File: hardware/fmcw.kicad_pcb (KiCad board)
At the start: 4 copper layers, 147.8 x 58.9 mm, 414 parts, among them CON1 BARREL_JACK, J1 SD_Card, J2 USB_B_Micro, J3 SMA, J4 SMA, J5 SMA, P1 CONN_02X04, P2 CONN_02X04, Q1 DNP(RE1C002UN), Q2 RE1C002UN, SW1 SW_PUSH, U1 LP5907MFX-3.3, U10 LP5907MFX-3.0, U11 LTC2292, U12 ADF4158, U13 TLV172DCK, U14 PAT1220-3dB, U15 HMC431LP4, U16 PD4859J5050S2HF, U17 PAT1220-5dB, U18 SE5004L, U19 DC4759J5020AHF, U2 LP5907MFX-1.8, U20 PAT1220-6dB, U22 TRF37A73, U23 SKY65404, U24 TRF37A73, U25 SKY65404, U26 TPS5420D, U27 TPS5420D, U28 TPS560200, U29 LP2985A-10DBVR, U3 KT2520K-T, U30 TPS7A7001DDA, U31 TPS7A91, U32 TPS7A91, U33 LP5907MFX-3.0, U34 TPS7A91, U35 5400BL15B050E, U36 5400BL15B050E, U37 5400BL15B050E, U38 ADL5802, U39 ADA4940-2, U4 NC7SVU04P5X, U5 NB3N551, U6 XC7A15T-FTG256, U7 W25Q32JV, U8 93LCxxB, U9 FT2232H, Y1 12MHz

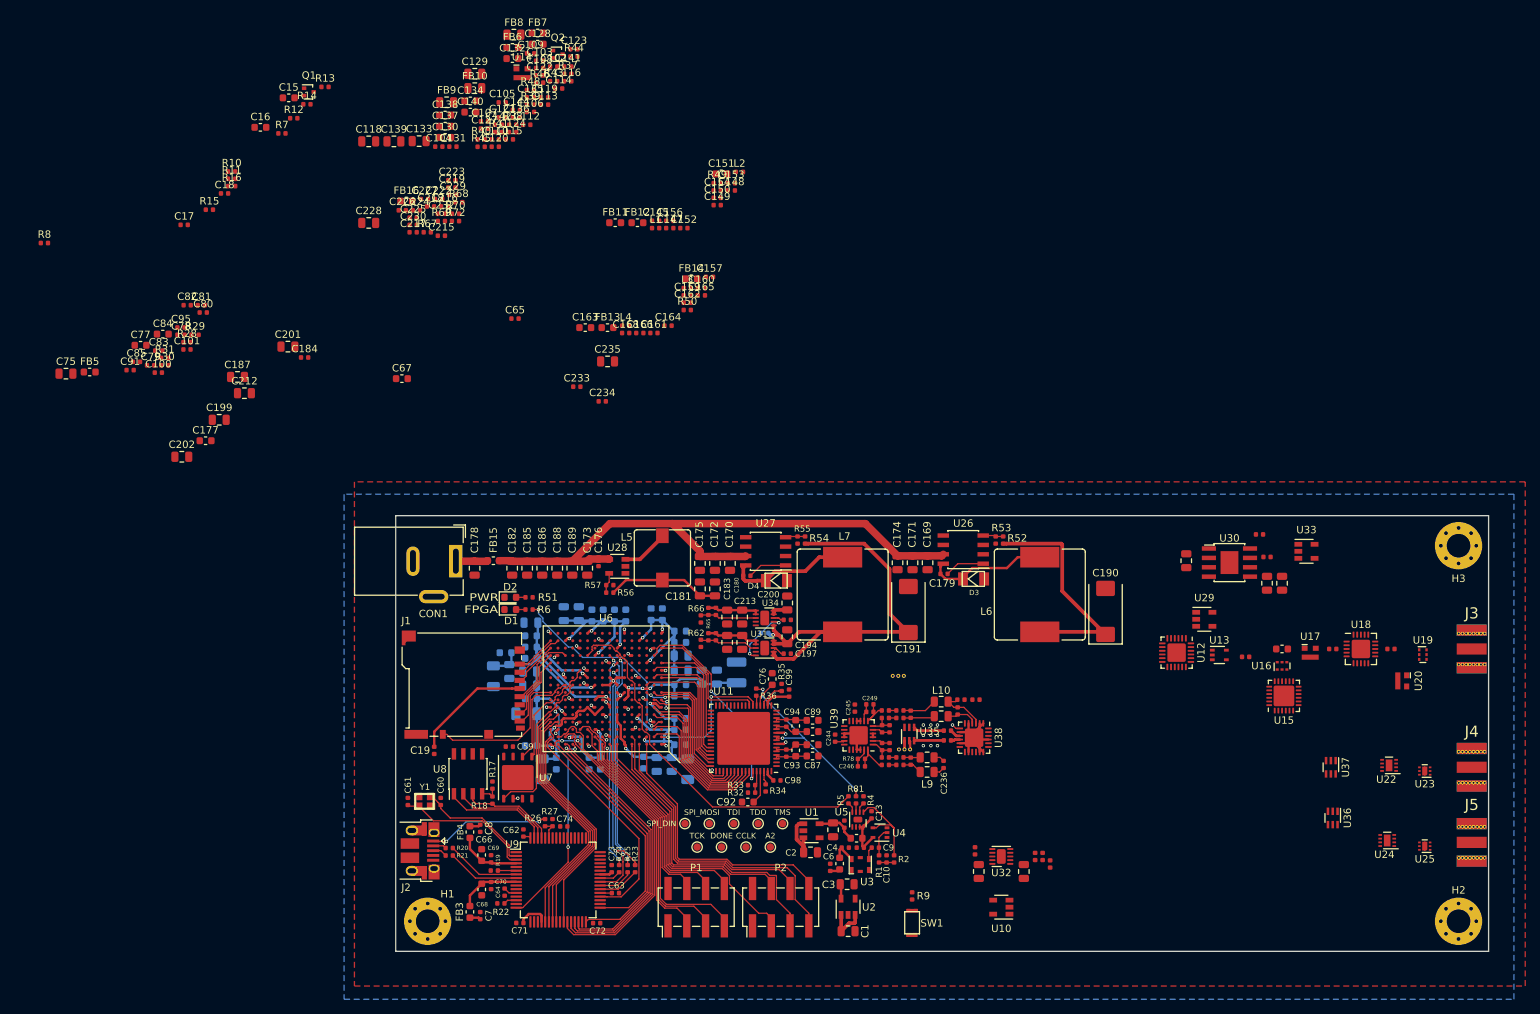
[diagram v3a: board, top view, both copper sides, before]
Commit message: Placed/routed all FPGA external components.
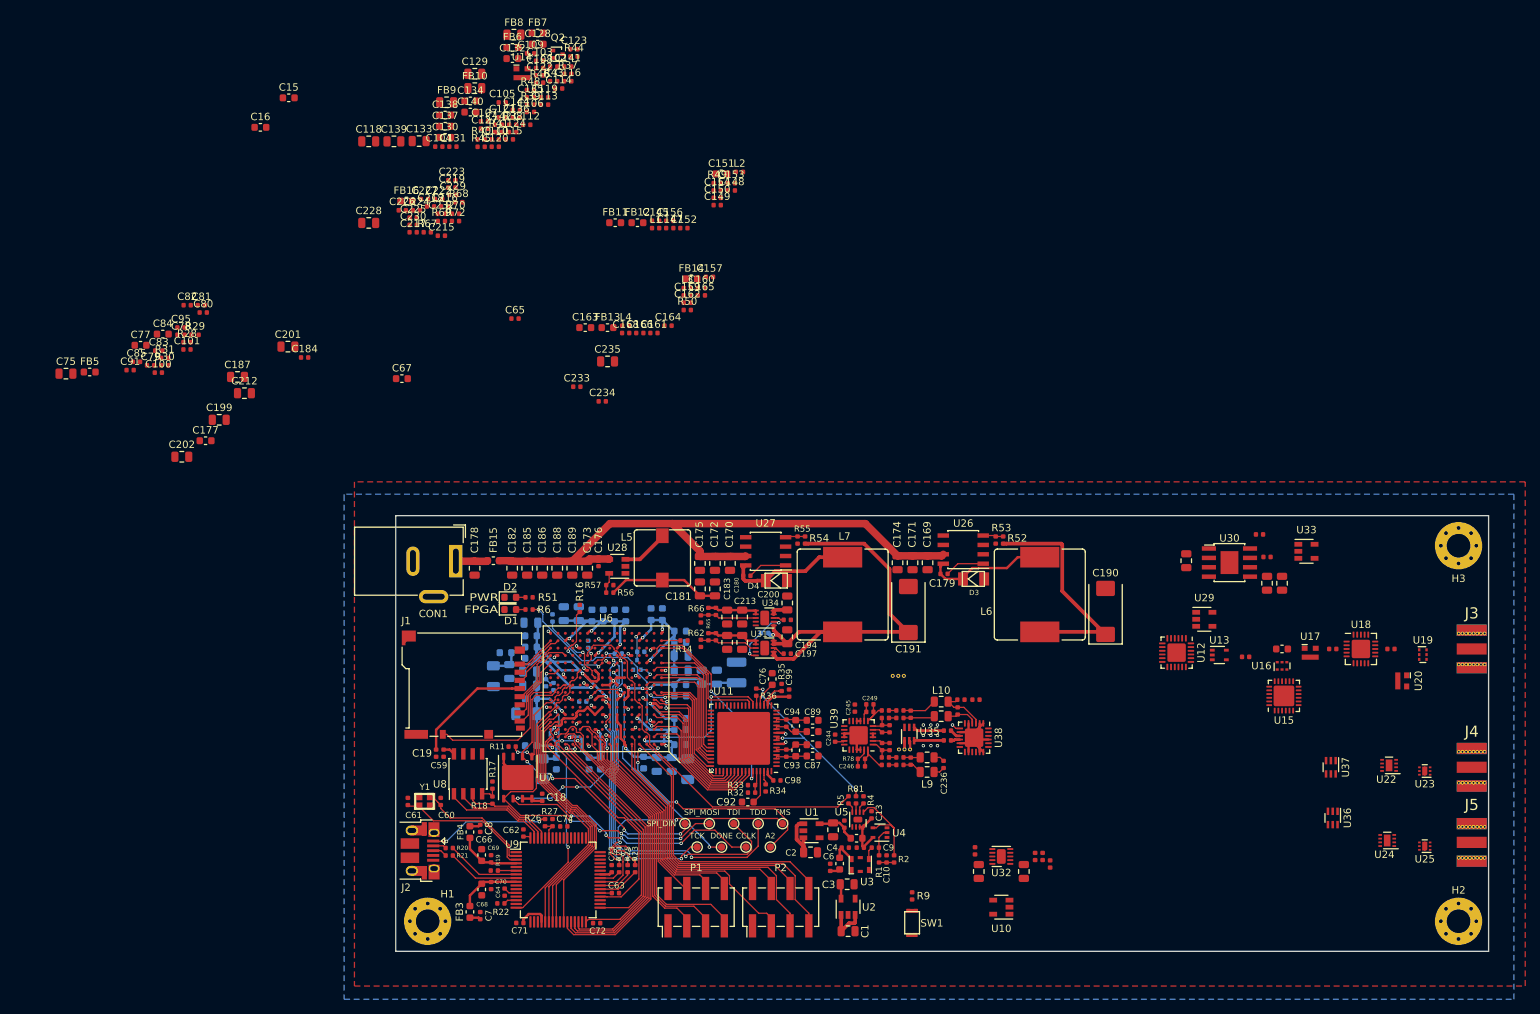
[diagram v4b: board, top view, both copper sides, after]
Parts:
- C17, Q1, R10, R12, R13, R15, R7, R8: moved to B.Cu
- moved C18 92.3 mm to (106.2, 125.7), turned to 270 degrees
- moved R8 91.3 mm to (107.7, 110.7), turned to 270 degrees
- moved Q1 89.3 mm to (119.0, 107.8), turned to 90 degrees
- moved R14 88.7 mm to (125.3, 104.5)
- moved R12 88.1 mm to (111.7, 112.8)
- moved R11 85.7 mm to (102.1, 118.9)
- moved C17 84.6 mm to (119.5, 106.0)
- moved R13 83.4 mm to (112.4, 105.0), turned to 90 degrees
- moved R7 82.4 mm to (106.7, 110.2), turned to 90 degrees
- moved R15 81.6 mm to (116.5, 106.3)
- moved R10 74.4 mm to (107.6, 101.5), turned to 270 degrees
- moved R16 74.0 mm to (111.3, 100.2), turned to 270 degrees
- moved C59 8.93 mm to (92.8, 119.8), turned to 270 degrees
- moved C19 0.46 mm to (91.8, 119.8)
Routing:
- net /fpga/CCLK: track 0.66 -> 58.4 mm, vias 1 -> 8
- net Net-(TP9-Pad1): track 0.00 -> 33.8 mm, vias 0 -> 4
- net Net-(R12-Pad2): track 0.00 -> 33.5 mm, vias 0 -> 3
- net /fpga/SPI_MOSI: track 21.5 -> 52.4 mm, vias 0 -> 4
- net /fpga/TMS: track 28.5 -> 57.7 mm, vias 2 -> 4
- net /fpga/SPI_DIN: track 13.7 -> 41.4 mm, vias 0 -> 4
- net /fpga/TDO: track 34.5 -> 61.2 mm, vias 2 -> 4
- net /fpga/TDI: track 29.5 -> 51.7 mm, vias 2 -> 3
- net /fpga/M0: track 0.00 -> 11.8 mm, vias 0 -> 2
- net /fpga/INIT_B: track 0.00 -> 10.5 mm, vias 0 -> 1
- net /fpga/TCK: track 29.0 -> 39.4 mm, vias 2 -> 4
- net /3V3D: track 143.7 -> 148.4 mm
- net /fpga/ADF_DONE: track 0.00 -> 3.86 mm, vias 0 -> 1
- net Net-(R7-Pad2): track 0.00 -> 3.74 mm, vias 0 -> 1
- net GND: track 48.6 -> 52.2 mm
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
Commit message: Better MFNs for RF DC blocking caps.
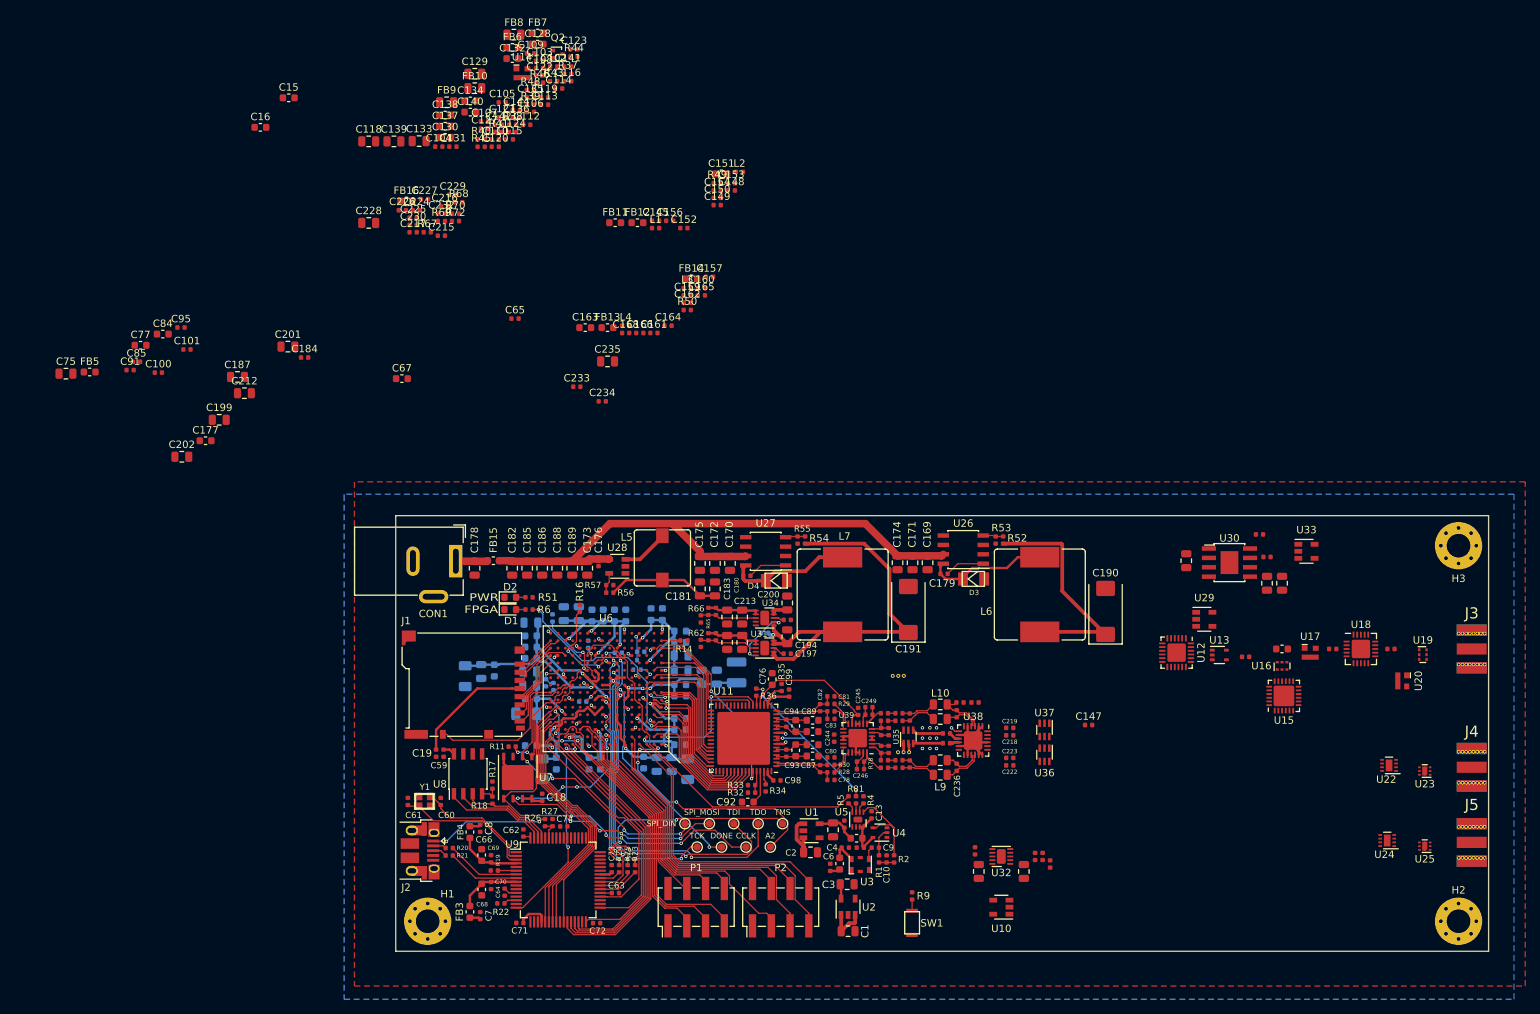
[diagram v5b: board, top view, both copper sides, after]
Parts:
- moved C222 108.8 mm to (169.4, 121.4)
- moved C223 108.6 mm to (169.4, 120.4)
- moved C78 106.6 mm to (145.2, 123.4), turned to 180 degrees
- moved C218 106.1 mm to (169.4, 117.3)
- moved C79 105.7 mm to (143.8, 121.9), turned to 90 degrees
- moved R30 105.1 mm to (145.2, 121.3)
- moved C219 105.1 mm to (169.4, 116.3)
- moved R28 104.8 mm to (145.2, 122.4)
- moved C80 104.1 mm to (145.2, 120.3)
- moved C83 103.7 mm to (145.2, 115.1)
- moved R31 102.0 mm to (145.2, 114.1)
- moved C82 101.5 mm to (143.8, 113.6), turned to 270 degrees
- moved C81 100.3 mm to (145.2, 112.1), turned to 180 degrees
- moved R29 99.4 mm to (145.2, 113.1)
- moved C147 87.9 mm to (180.1, 116.0)
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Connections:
- net Net-(C218-Pad2) renamed /mixer/RF1a+
- net Net-(C219-Pad2) renamed /mixer/RF1a-
- net Net-(C222-Pad2) renamed /mixer/RF2a+
- net Net-(C223-Pad2) renamed /mixer/RF2a-
- net Net-(C238-Pad1) renamed /if/IF2a-
- net Net-(C238-Pad2) renamed /if/IF2a+
- net Net-(C239-Pad1) renamed /if/IF1a-
- net Net-(C239-Pad2) renamed /if/IF1a+
- net Net-(C240-Pad1) renamed /if/IF2b-
- net Net-(C241-Pad1) renamed /if/IF2b+
- net Net-(C242-Pad1) renamed /if/IF1b-
- net Net-(C243-Pad1) renamed /if/IF1b+
- net Net-(C78-Pad2) renamed /fpga/adc/AINA+
- net Net-(C79-Pad2) renamed /fpga/adc/AINA-
- net Net-(C81-Pad2) renamed /fpga/adc/AINB+
- net Net-(C82-Pad2) renamed /fpga/adc/AINB-
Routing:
- net /ADC_VCM2: track 3.47 -> 19.1 mm
- net /fpga/adc/AINB+: track 0.00 -> 8.37 mm
- net /fpga/adc/AINA+: track 0.00 -> 8.35 mm
- net /fpga/adc/AINB-: track 0.00 -> 8.07 mm
- net /fpga/adc/AINA-: track 0.00 -> 8.05 mm
- net /1V8: track 56.6 -> 51.3 mm
- net /if/IF2+: track 1.50 -> 5.30 mm
- net /ADC2-: track 0.00 -> 3.48 mm
- net /ADC1-: track 0.00 -> 3.48 mm
- net /if/IF2-: track 1.48 -> 4.85 mm
- net /ADC2+: track 0.00 -> 3.25 mm
- net /ADC1+: track 0.00 -> 3.25 mm
- net /if/IF2a-: track 2.28 -> 4.88 mm
- net /if/IF2a+: track 2.67 -> 4.58 mm
- net /fpga/PROGRAM_B: track 0.00 -> 1.55 mm
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
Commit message: Completed transmitter placement/routing.
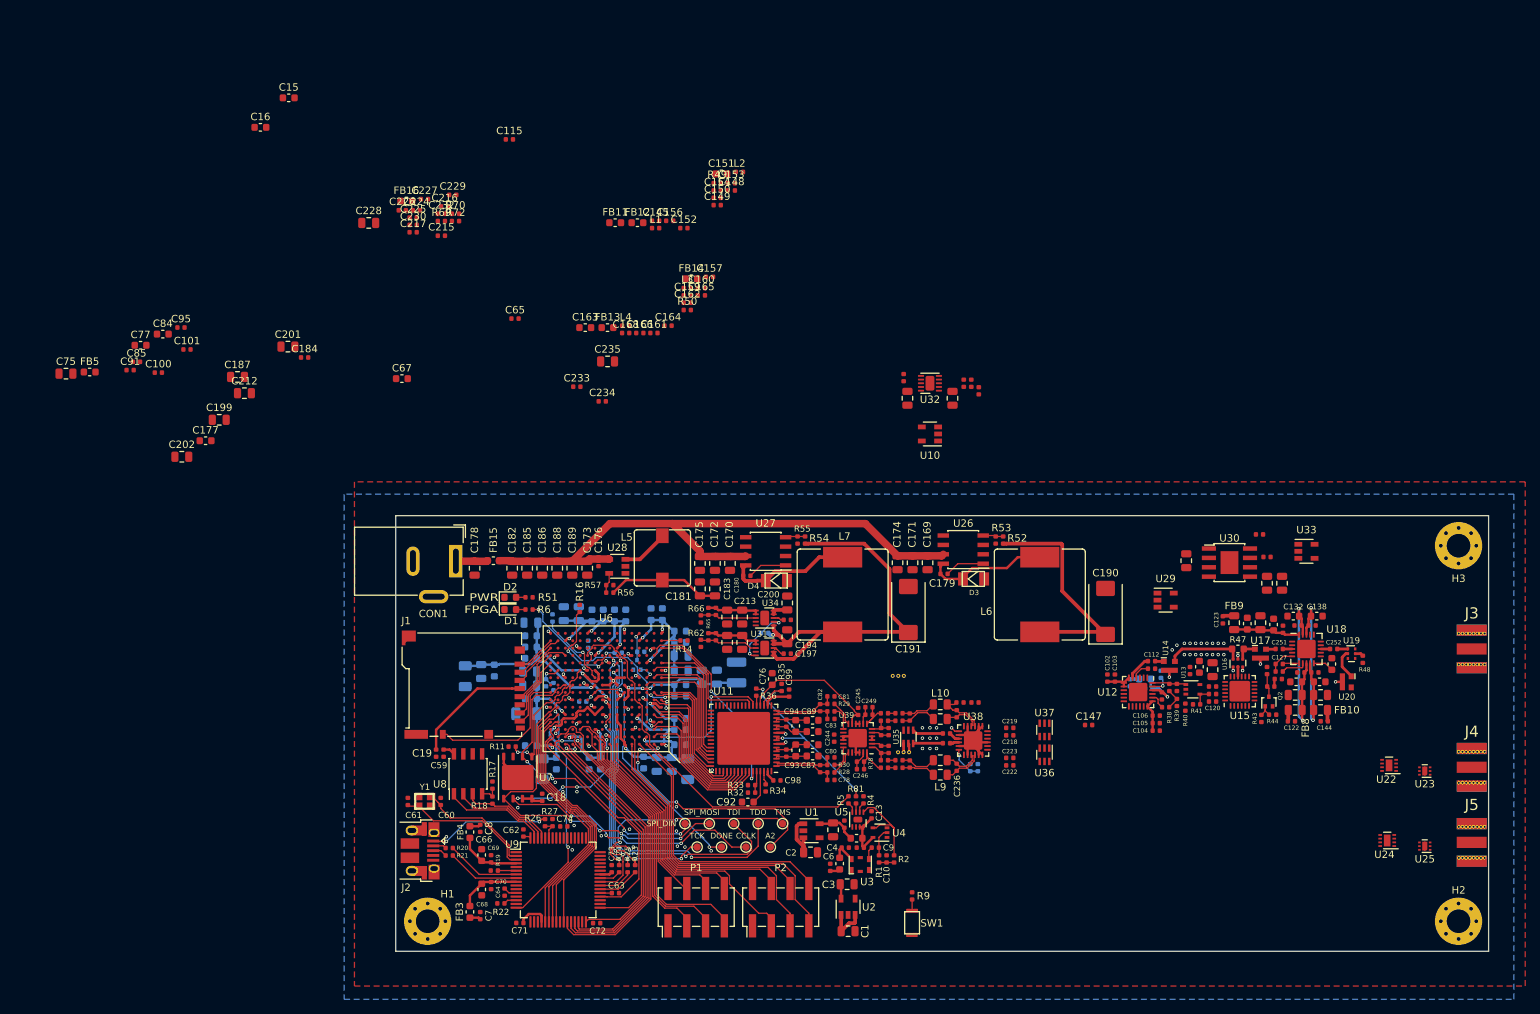
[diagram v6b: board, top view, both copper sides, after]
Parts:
- C108, C113, FB6, R37, R67, R68: moved to B.Cu
- moved C139 146.0 mm to (211.5, 111.9), turned to 180 degrees
- moved FB10 142.0 mm to (211.5, 113.9), turned to 180 degrees
- moved C137 140.3 mm to (213.0, 107.7), turned to 90 degrees
- moved C133 140.2 mm to (208.0, 111.9)
- moved FB8 139.7 mm to (208.0, 113.9), turned to 180 degrees
- moved C140 138.3 mm to (211.3, 110.1), turned to 180 degrees
- moved C144 137.0 mm to (212.0, 115.4), turned to 180 degrees
- moved C134 136.6 mm to (208.2, 110.1)
- moved R48 136.4 mm to (217.2, 107.1), turned to 90 degrees
- moved C138 136.0 mm to (210.9, 101.2), turned to 180 degrees
- moved C118 134.7 mm to (196.8, 108.5), turned to 270 degrees
- moved C122 134.1 mm to (207.5, 115.4)
- moved C142 133.0 mm to (210.7, 108.8), turned to 180 degrees
- moved Q2 130.1 mm to (204.5, 112.8), turned to 90 degrees
- moved C130 130.0 mm to (205.1, 102.4), turned to 90 degrees
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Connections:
- net Net-(C218-Pad1) renamed /mixer/RF1b-
- net Net-(C219-Pad1) renamed /mixer/RF1b+
- net Net-(C222-Pad1) renamed /mixer/RF2b-
- net Net-(C223-Pad1) renamed /mixer/RF2b+
- C218 pad 2: /mixer/RF1a+ -> /mixer/RF1a-
- C219 pad 2: /mixer/RF1a- -> /mixer/RF1a+
- C222 pad 2: /mixer/RF2a+ -> /mixer/RF2a-
- C223 pad 2: /mixer/RF2a- -> /mixer/RF2a+
- U36 pad 3: /mixer/RF2a- -> /mixer/RF2a+
- U36 pad 4: /mixer/RF2a+ -> /mixer/RF2a-
- U37 pad 3: /mixer/RF1a- -> /mixer/RF1a+
- U37 pad 4: /mixer/RF1a+ -> /mixer/RF1a-
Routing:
- net Net-(C138-Pad2): track 0.00 -> 27.2 mm, vias 0 -> 2
- net Net-(C132-Pad2): track 0.00 -> 27.1 mm, vias 0 -> 2
- net Net-(R47-Pad2): track 0.00 -> 10.3 mm
- net /3V3A: track 1.00 -> 10.3 mm
- net Net-(C128-Pad1): track 0.00 -> 9.08 mm
- net Net-(C124-Pad2): track 0.00 -> 6.84 mm
- net Net-(C108-Pad1): track 0.00 -> 6.29 mm, vias 0 -> 1
- net /5V: track 0.00 -> 5.90 mm
- net Net-(C110-Pad1): track 0.00 -> 4.61 mm
- net Net-(R67-Pad2): track 0.00 -> 4.56 mm, vias 0 -> 1
- net GND: track 52.2 -> 56.4 mm, vias 38 -> 77
- net Net-(U19-Pad2): track 0.00 -> 4.06 mm
- net Net-(C124-Pad1): track 0.00 -> 3.46 mm
- net Net-(C112-Pad2): track 0.00 -> 3.35 mm
- net Net-(C110-Pad2): track 0.00 -> 3.03 mm
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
